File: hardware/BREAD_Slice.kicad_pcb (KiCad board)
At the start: 2 copper layers, 70 x 100 mm, 54 parts, among them J1 I2C_01x04, J2 Conn_01x10_Female, J3 Conn_01x02_Female, J4 Tab_Amp_1217861-1, J5 Tab_Amp_1217861-1, J6 Tab_Amp_1217861-1, J7 Tab_Amp_1217861-1, Q1 AO4882, Q2 2N7002, U2 LM234Z-3, U3 NSL-32, U4 BQ24650RVAT, U5 NSL-32

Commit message: fix(hw): re-point stale library nicknames
These parts exist in KiCad-Master-Lib; the boards referenced libraries that no
longer exist (kml-custom, KML-Custom, and SparkFun libraries that never
contained the part) or names the library has since changed.

KiCad embeds footprint geometry in the .kicad_pcb, so the boards rendered and
fabricated correctly and the rot stayed invisible -- it only surfaces on
update-from-library, or when a generator tries to resolve a nickname.

Nickname/name only. No geometry is changed:

  KML-Custom:CDBA-G -> KMLib_Passives_SMD:CDBA-G
  KML-Custom:RVA16_2P14X2P14 -> KMLib_IC_SMD:RVA16_2P14X2P14
  KML-Custom:Thermal Pad -> KMLib_Mounting:Thermal_Pad
  SparkFun-DiscreteSemi:AP63205 -> KMLib_IC_Power:AP63205WU-7_Buck_Regulator
  SparkFun-Fuse:Thermal Pad -> KMLib_Mounting:Thermal_Pad
  SparkFun-LED:WS2812-5050-4PIN -> KMLib_IC_SMD:WS2812-5050-4PIN
  kml-custom:BQ24650RVAT -> KMLib_IC_Power:BQ24650RVAT_Charger_Controller

Only references that failed to resolve were touched. Generic parts (<=4 pins)
and KiCad *-rescue libraries are deliberately excluded: fingerprint matching
cannot distinguish a 2-pin resistor from a 2-pin capacitor, so those are being
done by hand.
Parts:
- D1: footprint SparkFun-LED:WS2812-5050-4PIN -> KMLib_IC_SMD:WS2812-5050-4PIN
- D3: footprint KML-Custom:CDBA-G -> KMLib_Passives_SMD:CDBA-G
- HS1: footprint SparkFun-Fuse:Thermal Pad -> KMLib_Mounting:Thermal_Pad
- U4: footprint KML-Custom:RVA16_2P14X2P14 -> KMLib_IC_SMD:RVA16_2P14X2P14
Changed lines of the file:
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@@
 		(embedded_fonts no)
 	)
-	(footprint "SparkFun-Fuse:Thermal Pad"
+	(footprint "KMLib_Mounting:Thermal_Pad"
 		(layer "F.Cu")
 		(at 131.35 121.355)
@@
 		(embedded_fonts no)
 	)
-	(footprint "SparkFun-LED:WS2812-5050-4PIN"
+	(footprint "KMLib_IC_SMD:WS2812-5050-4PIN"
 		(locked yes)
 		(layer "F.Cu")
@@
 		)
 	)
-	(footprint "KML-Custom:RVA16_2P14X2P14"
+	(footprint "KMLib_IC_SMD:RVA16_2P14X2P14"
 		(layer "B.Cu")
 		(at 149.4063 63.7063 180)
@@
 		)
 	)
-	(footprint "KML-Custom:CDBA-G"
+	(footprint "KMLib_Passives_SMD:CDBA-G"
 		(layer "B.Cu")
 		(at 161.7 63.5)

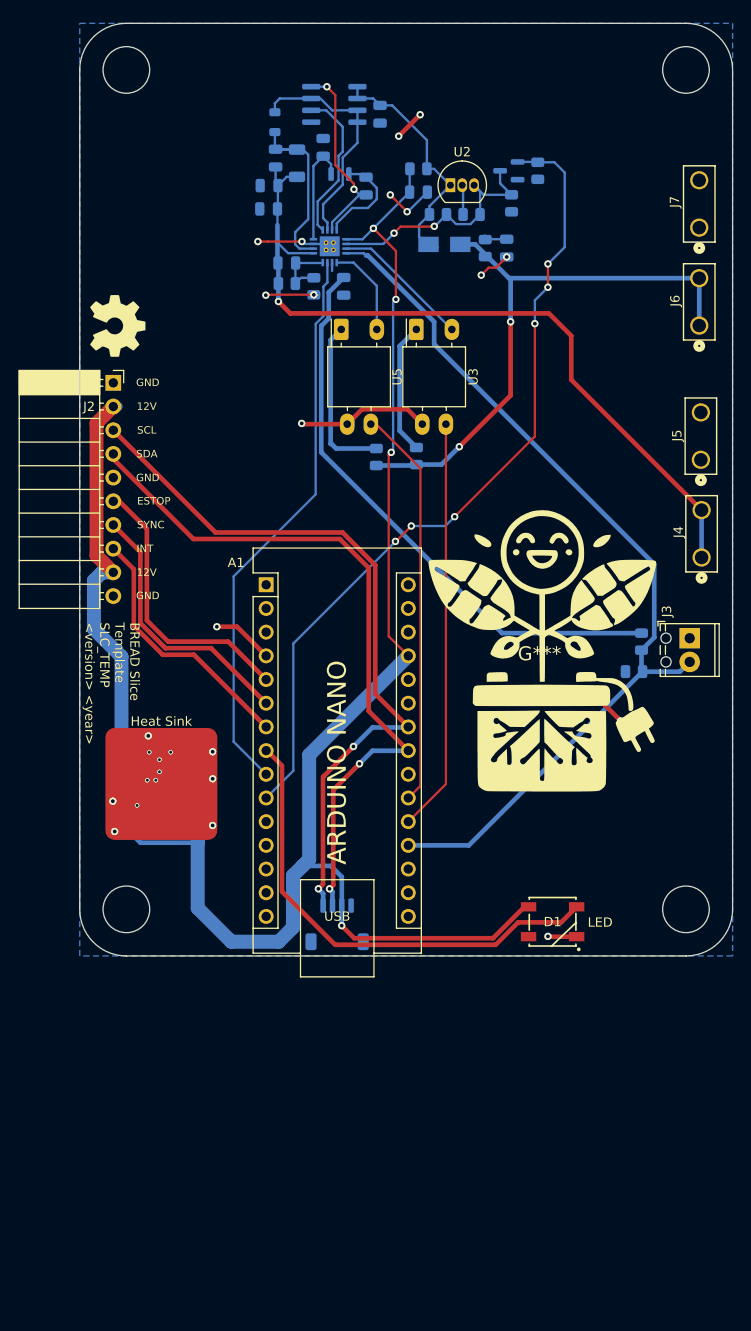
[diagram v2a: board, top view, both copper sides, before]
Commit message: feat(hw): redesign charger stage from the BQ24650 reference design
Rebuild the charger sheet against the BQ24650 datasheet and the
BQ24650EVM-639 reference design: PDS1040-13 and ZLLS350TA Schottky
diodes, SI7288DP-T1-GE3 dual MOSFET, input and output filtering, and
test points per the EVM. Every symbol now resolves from
KiCad-Master-Lib; the *-rescue, kml-custom and SparkFun references are
gone, and the top sheet drops the unused I2C header.

The bootstrap diode is oriented REGN -> BTST as the datasheet requires,
and the BQ24650 VCC net carries a PWR_FLAG since it is fed through the
input filter resistors. ERC is clean at all severities.

The PCB is cleared for re-layout: the Nano socket, buck stage and
mechanicals are placed, nothing is routed, and DRC schematic parity
reports 66 missing footprints until layout lands.
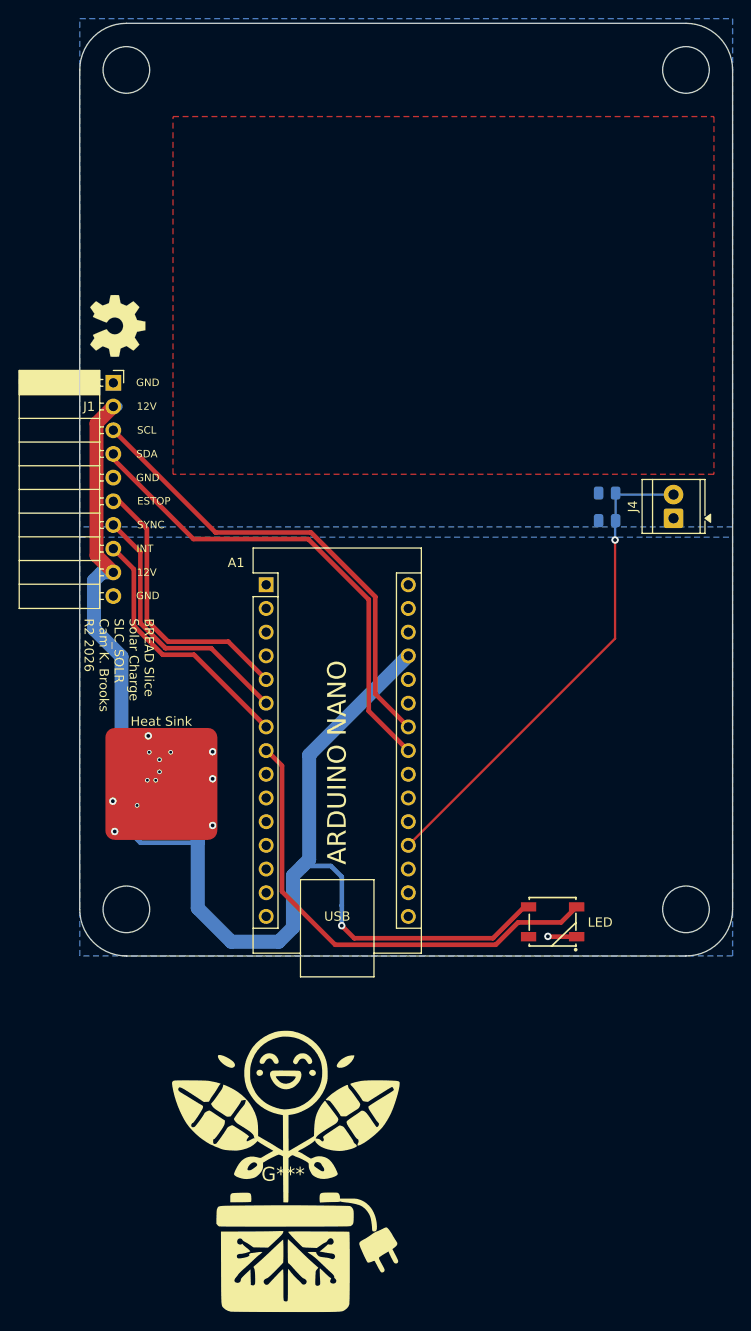
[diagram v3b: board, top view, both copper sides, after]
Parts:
- removed C10: 2.2uF, Capacitor_SMD:C_0805_2012Metric
- removed C11: 0.47u, Capacitor_SMD:C_0805_2012Metric
- removed C12: 4.7uF, Capacitor_SMD:C_0805_2012Metric
- removed C13: 22pF, Capacitor_SMD:C_0805_2012Metric
- removed C14, C7: 1uF, Capacitor_SMD:C_0805_2012Metric
- removed C5, C8: 0.1uF, Capacitor_SMD:C_0805_2012Metric
- removed C6: 2.2u, Capacitor_SMD:C_0805_2012Metric
- removed C9: 10uF, Capacitor_SMD:C_0805_2012Metric
- removed D2: BAT54C, Package_TO_SOT_SMD:SOT-23
- removed D3: CDBA140-G, KMLib_Passives_SMD:CDBA-G
- removed the J1 at (150.2, 136.4)
- removed J3: Conn_01x02_Female, TerminalBlock_Phoenix:TerminalBlock_Phoenix_MPT-0,5-2-2.54_1x02_P2.54mm_Horizontal
- removed J5, J6, J7: Tab_Amp_1217861-1, KML-Custom:CONN_1217861-1_TEC
- removed L2: 22uH, Inductor_SMD:L_0805_2012Metric
- removed Q1: AO4882, Package_SO:SOIC-8_3.9x4.9mm_P1.27mm
- removed Q2: 2N7002, Package_TO_SOT_SMD:SOT-23
- removed R1: 2, Resistor_SMD:R_0805_2012Metric
- removed R10: 100k, Resistor_SMD:R_0805_2012Metric
- removed R11, R12, R2: 10k, Resistor_SMD:R_0805_2012Metric
- removed R5: 169k, Resistor_SMD:R_0805_2012Metric
- removed R6: 10.6k, Resistor_SMD:R_0805_2012Metric
- removed R7: 80m - sense res, Resistor_SMD:R_1206_3216Metric
- removed R8: 20, Resistor_SMD:R_0805_2012Metric
- removed R9: 300k, Resistor_SMD:R_0805_2012Metric
- removed Rset1: 1k, Resistor_SMD:R_0805_2012Metric
- removed U2: LM234Z-3, Package_TO_SOT_THT:TO-92_Inline
- removed U3, U5: NSL-32, OptoDevice:Luna_NSL-32
- removed U4: BQ24650RVAT, KMLib_IC_SMD:RVA16_2P14X2P14
- J4: value Tab_Amp_1217861-1 -> Conn_01x02_Female; footprint KML-Custom:CONN_1217861-1_TEC -> TerminalBlock_TE-Connectivity:TerminalBlock_TE_282834-2_1x02_P2.54mm_Horizontal
- U1: value ~ -> AP63205WU-7; footprint Package_TO_SOT_SMD:TSOT-23-6 -> KMLib_IC_SMD:SOIC_05WU-7_DIO
- moved G*** 62.2 mm to (144.4, 163.2)
- moved R4 16.4 mm to (179.1, 93.1)
- moved R3 16.3 mm to (179.1, 90.2), turned to 0 degrees
- moved J4 5.17 mm to (186.3, 92.9)
- renumbered J2 to J1
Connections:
- A1 pad 20: /STAT1_IN -> /STAT2_IN
- A1 pad 21: /STAT2_IN -> /STAT1_IN
- J4 pad 1: /BQ24650 Solar Charger/BatteryOut -> GND
- J4 pad 2: /BQ24650 Solar Charger/BatteryOut -> /BAT_RTD
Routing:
- net /CHRG_EN: track 88.0 -> 0.00 mm, vias 6 -> 0
- net /BQ24650 Solar Charger/BatteryOut: track 83.8 -> 0.00 mm, vias 1 -> 0
- net /BQ24650 Solar Charger/VREF: track 63.0 -> 0.00 mm
- net /BQ24650 Solar Charger/SolarIn: track 62.4 -> 0.00 mm, vias 2 -> 0
- net /TERM_EN: track 60.5 -> 0.00 mm
- net +5V: track 167.3 -> 107.9 mm, vias 4 -> 1
- net GND: track 69.7 -> 19.6 mm, vias 28 -> 14
- net /BAT_RTD: track 98.7 -> 53.3 mm, vias 0 -> 1
- net /STAT1_IN: track 44.3 -> 0.00 mm
- net /STAT2_IN: track 43.2 -> 0.00 mm
- net /I2C_CLK: track 78.5 -> 50.9 mm, vias 2 -> 0
- net /BQ24650 Solar Charger/MPPSET: track 27.5 -> 0.00 mm, vias 2 -> 0
- net /BQ24650 Solar Charger/HIDRV_D: track 25.3 -> 0.00 mm
- net /I2C_DAT: track 76.6 -> 52.1 mm, vias 2 -> 0
- net /BQ24650 Solar Charger/PH: track 24.1 -> 0.00 mm
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- added copper zone on B.Cu, net /BQ24650 Solar Charger/PGND
- added copper zone on F.Cu, net /BQ24650 Solar Charger/PGND
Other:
- board text added: "BREAD Slice Solar Charge SLC_SOLR Cam K. Brooks R2 2026"
- board text removed: "BREAD Slice Template SLC_TEMP <version> <year>"

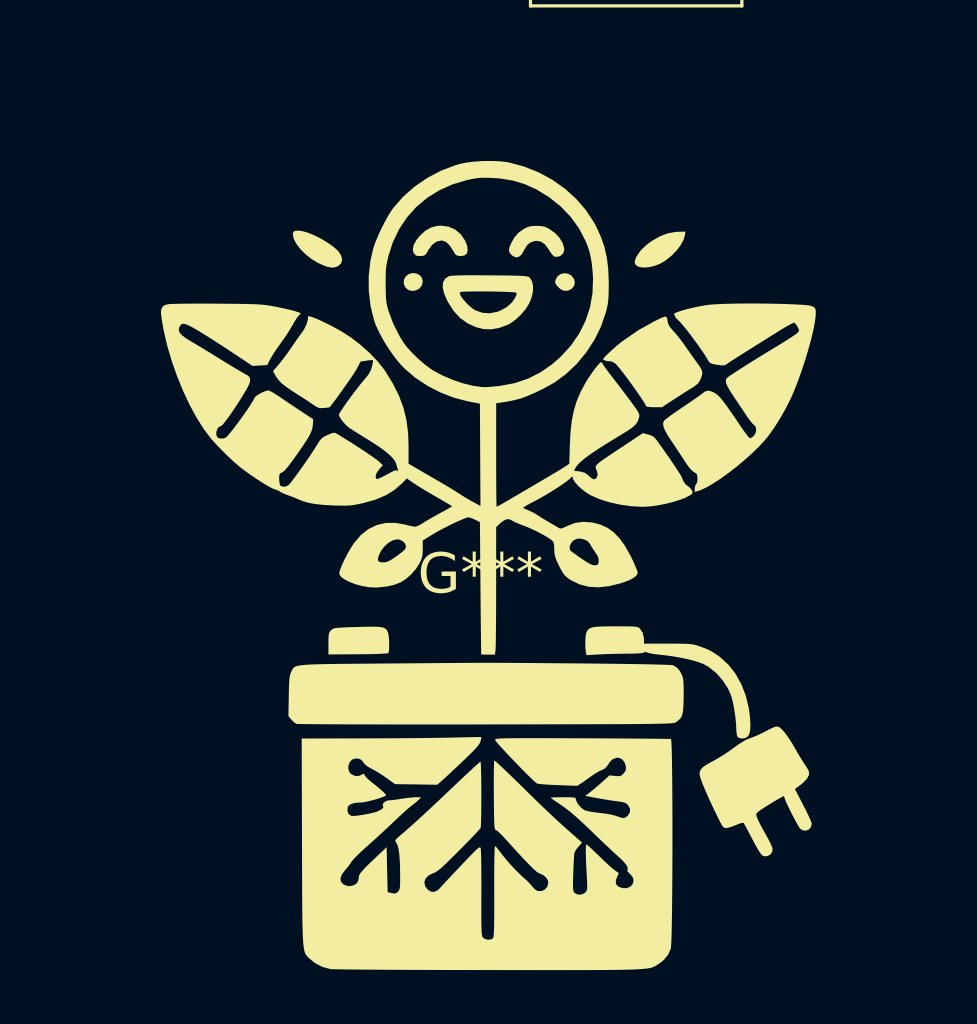
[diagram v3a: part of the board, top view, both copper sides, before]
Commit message: fix(hw): drop the library-less LOGO footprint from the PCB
The happy-solar-plant artwork was placed as a footprint with no
library nickname, so nothing can resolve it and validate-board fails.
Remove it for now; it comes back from a proper library during layout.
The artwork itself stays in hardware/happy-solar-plant.png.
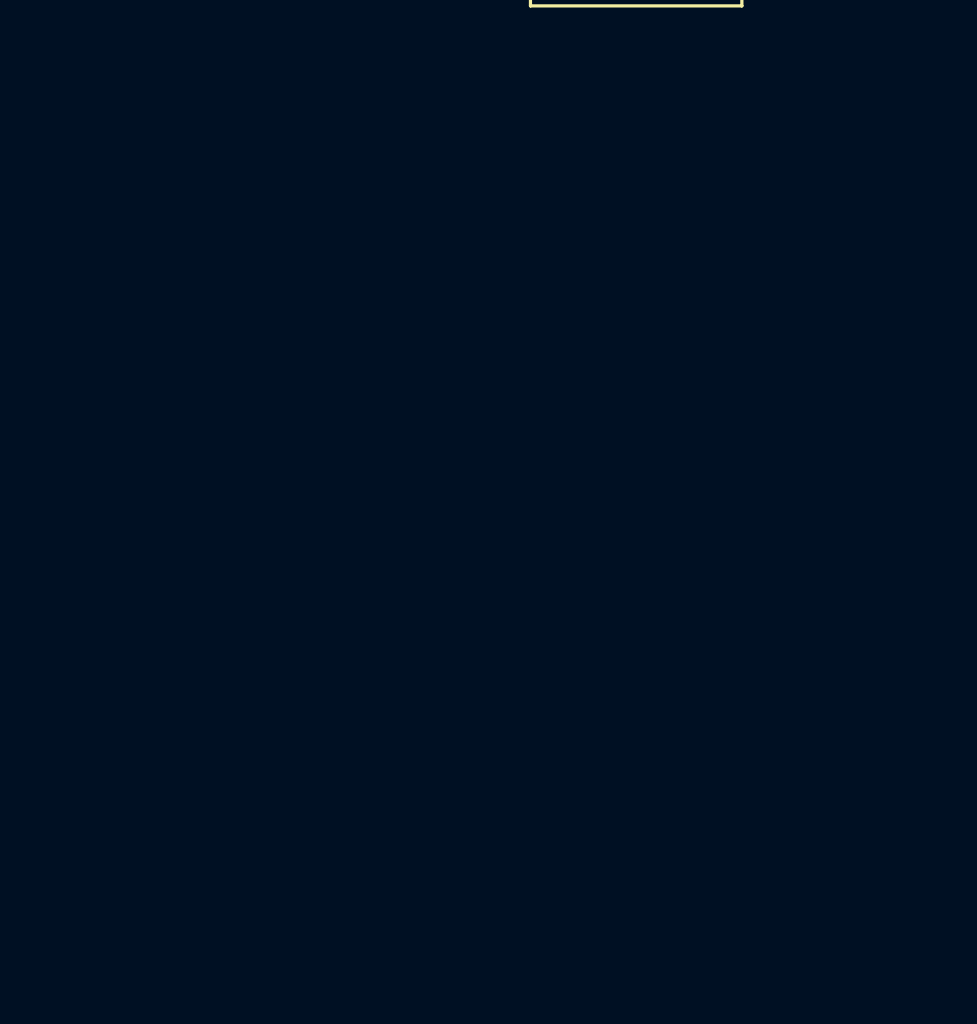
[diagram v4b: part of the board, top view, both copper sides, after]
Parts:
- removed G***: LOGO, LOGO
